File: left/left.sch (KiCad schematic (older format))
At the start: 41 parts, among them J1 Modulo-Jack, J2 Modulo-Jack, J3 Modulo-Jack, SW1 SW_Push, SW10 SW_Push, SW11 SW_Push, SW12 SW_Push, SW13 SW_Push, SW14 SW_Push, SW15 SW_Push, SW16 SW_Push, SW17 SW_Push, SW18 SW_Push, SW19 SW_Push, SW2 SW_Push, SW20 SW_Push, SW21 SW_Push, SW22 SW_Push, SW23 SW_Push, SW24 SW_Push, SW25 SW_Push, SW26 SW_Push, SW27 SW_Push, SW28 SW_Push, SW29 SW_Push, SW3 SW_Push, SW30 SW_Push, SW31 SW_Push, SW32 SW_SPDT, SW33 SW_SPDT, SW4 SW_Push, SW5 SW_Push, SW6 SW_Push, SW7 SW_Push, SW8 SW_Push, SW9 SW_Push, U1 MCP23017_SP, U2 MCP23017_SP

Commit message: left: change address switch to DPDT
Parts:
- removed SW32, SW33: SW_SPDT, lib:SlideSwitch_SS-12D00, symbol Switch:SW_SPDT
- added SW32, SW33: SW_DPDT_x2, lib:SlideSwitch_IS2235, symbol Switch:SW_DPDT_x2
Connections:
- net A1: now also SW32.2 (B)
- net A2: now also SW33.2 (B)
- net GND: now also SW32.3 (C), SW33.3 (C)
- net VCC: now also SW32.1 (A), SW33.1 (A)
- no-connect marks 6 -> 14
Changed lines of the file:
@@
 Wire Wire Line
 	2700 5600 3000 5600
-$Comp
-L Switch:SW_SPDT SW32
-U 1 1 5CF616F7
-P 1550 6800
-F 0 "SW32" H 1550 7085 50  0000 C CNN
-F 1 "SW_SPDT" H 1550 6994 50  0000 C CNN
-F 2 "lib:SlideSwitch_SS-12D00" H 1550 6800 50  0001 C CNN
-F 3 "~" H 1550 6800 50  0001 C CNN
-	1    1550 6800
-	1    0    0    -1
-$EndComp
 Text GLabel 1350 6800 0    50   Output ~ 0
 A1
@@
 F 3 "" H 1750 6900 50  0001 C CNN
 	1    1750 6900
-	1    0    0    -1
-$EndComp
-$Comp
-L Switch:SW_SPDT SW33
-U 1 1 5CF62A7C
-P 2300 6800
-F 0 "SW33" H 2300 7085 50  0000 C CNN
-F 1 "SW_SPDT" H 2300 6994 50  0000 C CNN
-F 2 "lib:SlideSwitch_SS-12D00" H 2300 6800 50  0001 C CNN
-F 3 "~" H 2300 6800 50  0001 C CNN
-	1    2300 6800
 	1    0    0    -1
 $EndComp
@@
 	1    0    0    -1
 $EndComp
+$Comp
+L Switch:SW_DPDT_x2 SW32
+U 1 1 5CF7FADE
+P 1550 6800
+F 0 "SW32" H 1550 7085 50  0000 C CNN
+F 1 "SW_DPDT_x2" H 1550 6994 50  0000 C CNN
+F 2 "lib:SlideSwitch_IS2235" H 1550 6800 50  0001 C CNN
+F 3 "~" H 1550 6800 50  0001 C CNN
+	1    1550 6800
+	1    0    0    -1
+$EndComp
+$Comp
+L Switch:SW_DPDT_x2 SW33
+U 1 1 5CF804A5
+P 2300 6800
+F 0 "SW33" H 2300 7085 50  0000 C CNN
+F 1 "SW_DPDT_x2" H 2300 6994 50  0000 C CNN
+F 2 "lib:SlideSwitch_IS2235" H 2300 6800 50  0001 C CNN
+F 3 "~" H 2300 6800 50  0001 C CNN
+	1    2300 6800
+	1    0    0    -1
+$EndComp
+$Comp
+L Switch:SW_DPDT_x2 SW32
+U 2 1 5CF84163
+P 1550 7400
+F 0 "SW32" H 1550 7685 50  0000 C CNN
+F 1 "SW_DPDT_x2" H 1550 7594 50  0000 C CNN
+F 2 "lib:SlideSwitch_IS2235" H 1550 7400 50  0001 C CNN
+F 3 "~" H 1550 7400 50  0001 C CNN
+	2    1550 7400
+	1    0    0    -1
+$EndComp
+$Comp
+L Switch:SW_DPDT_x2 SW33
+U 2 1 5CF853BA
+P 2300 7400
+F 0 "SW33" H 2300 7685 50  0000 C CNN
+F 1 "SW_DPDT_x2" H 2300 7594 50  0000 C CNN
+F 2 "lib:SlideSwitch_IS2235" H 2300 7400 50  0001 C CNN
+F 3 "~" H 2300 7400 50  0001 C CNN
+	2    2300 7400
+	1    0    0    -1
+$EndComp
+NoConn ~ 1350 7400
+NoConn ~ 1750 7500
+NoConn ~ 1750 7300
+NoConn ~ 2500 7300
+NoConn ~ 2500 7500
+NoConn ~ 2100 7400
+NoConn ~ 2700 4700
+NoConn ~ 1300 4700
 $EndSCHEMATC

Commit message: last commit
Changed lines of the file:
@@
 NoConn ~ 2700 4700
 NoConn ~ 1300 4700
+$Comp
+L power:VCC #PWR051
+U 1 1 5CF90F28
+P 3400 7250
+F 0 "#PWR051" H 3400 7100 50  0001 C CNN
+F 1 "VCC" H 3417 7423 50  0000 C CNN
+F 2 "" H 3400 7250 50  0001 C CNN
+F 3 "" H 3400 7250 50  0001 C CNN
+	1    3400 7250
+	1    0    0    -1
+$EndComp
+$Comp
+L power:GND #PWR052
+U 1 1 5CF9147D
+P 3750 7250
+F 0 "#PWR052" H 3750 7000 50  0001 C CNN
+F 1 "GND" H 3755 7077 50  0000 C CNN
+F 2 "" H 3750 7250 50  0001 C CNN
+F 3 "" H 3750 7250 50  0001 C CNN
+	1    3750 7250
+	1    0    0    -1
+$EndComp
+$Comp
+L power:PWR_FLAG #FLG02
+U 1 1 5CF91B6C
+P 3750 7250
+F 0 "#FLG02" H 3750 7325 50  0001 C CNN
+F 1 "PWR_FLAG" H 3750 7423 50  0000 C CNN
+F 2 "" H 3750 7250 50  0001 C CNN
+F 3 "~" H 3750 7250 50  0001 C CNN
+	1    3750 7250
+	1    0    0    -1
+$EndComp
+$Comp
+L power:PWR_FLAG #FLG01
+U 1 1 5CF921EF
+P 3400 7250
+F 0 "#FLG01" H 3400 7325 50  0001 C CNN
+F 1 "PWR_FLAG" H 3400 7423 50  0000 C CNN
+F 2 "" H 3400 7250 50  0001 C CNN
+F 3 "~" H 3400 7250 50  0001 C CNN
+	1    3400 7250
+	1    0    0    1
+$EndComp
+$Comp
+L power:PWR_FLAG #FLG0101
+U 1 1 5CF94E79
+P 4200 7250
+F 0 "#FLG0101" H 4200 7325 50  0001 C CNN
+F 1 "PWR_FLAG" H 4200 7423 50  0000 C CNN
+F 2 "" H 4200 7250 50  0001 C CNN
+F 3 "~" H 4200 7250 50  0001 C CNN
+	1    4200 7250
+	1    0    0    -1
+$EndComp
+Text GLabel 4200 7250 3    50   Input ~ 0
+SCL
 $EndSCHEMATC

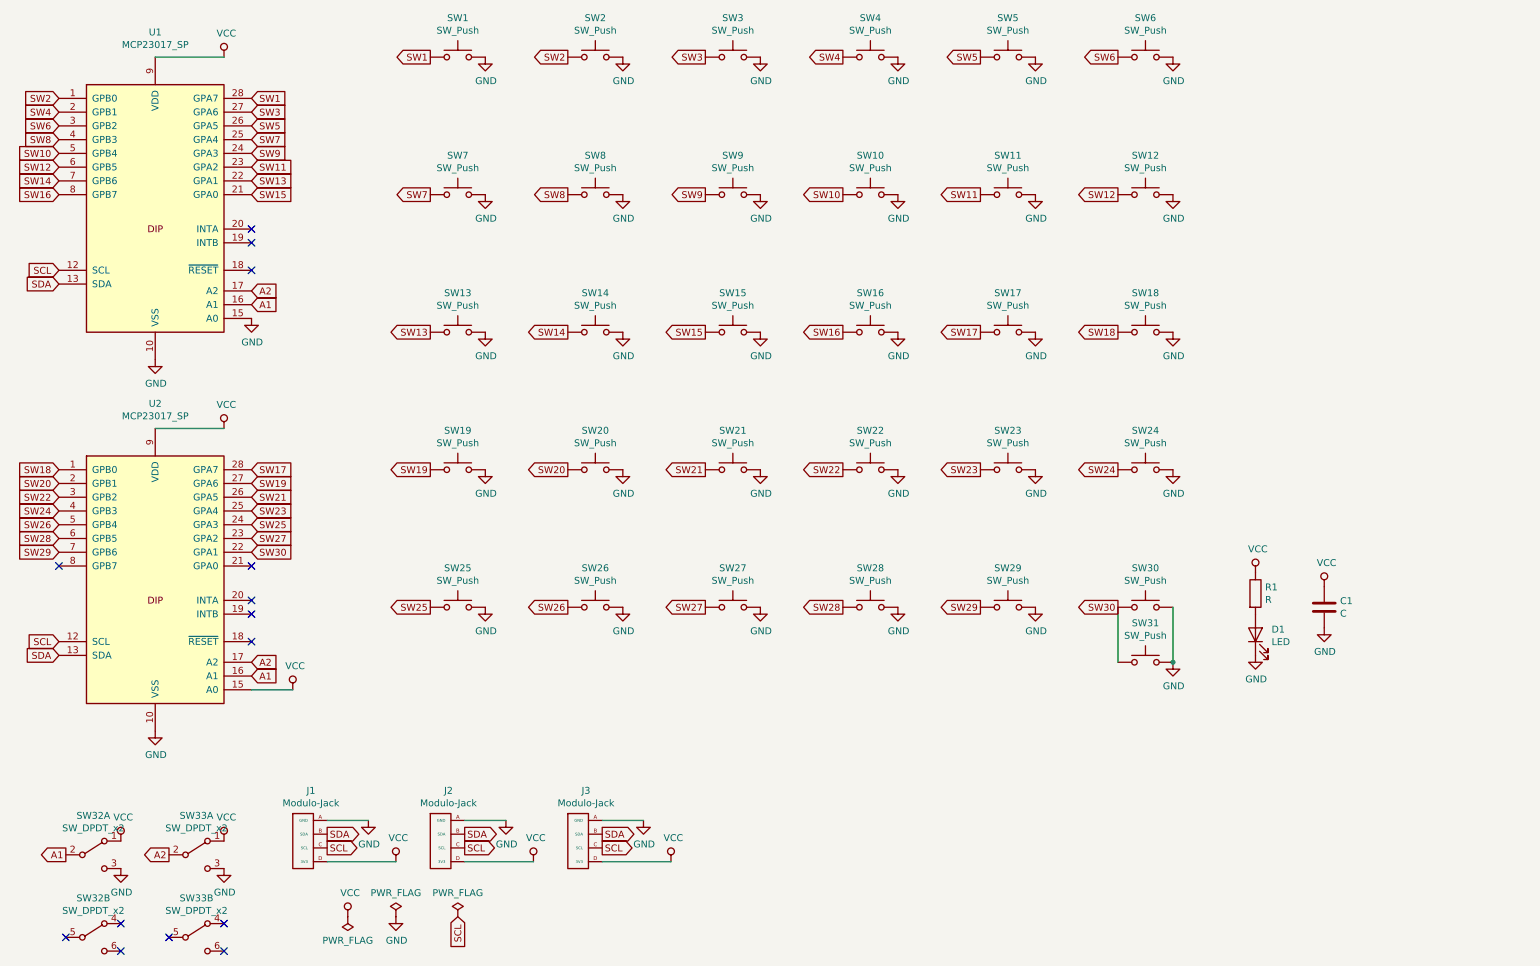
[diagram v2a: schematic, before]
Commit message: modify left to JIS layout
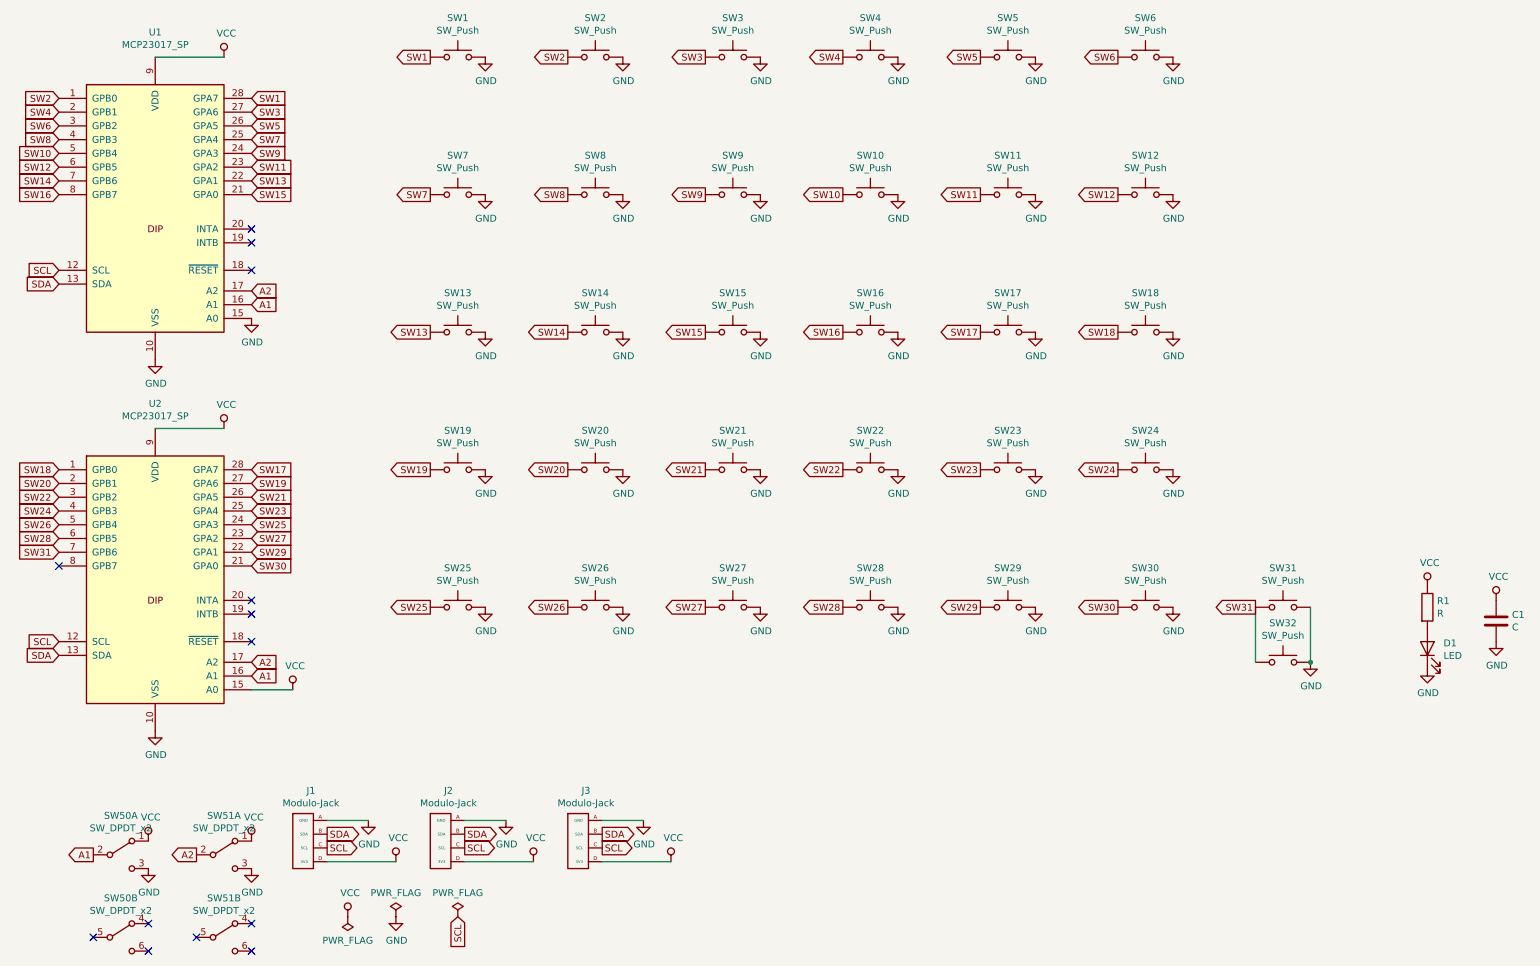
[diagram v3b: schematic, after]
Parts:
- added SW30: SW_Push, MX_Socket:MXOnly-1U-Hotswap, symbol Switch:SW_Push
- SW26: footprint MX_Socket:MXOnly-1.25U-Hotswap -> MX_Socket:MXOnly-1U-Hotswap
- renumbered SW30 to SW31, SW31 to SW32, SW32 to SW50, SW33 to SW51
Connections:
- net GND: now also SW31.1, SW32.1, SW30.1; no longer SW31.2, SW32.2
- net SW29: now also U2.22 (GPA1); no longer U2.7 (GPB6)
- net SW30: now also U2.21 (GPA0), SW30.2; no longer SW31.1, SW32.1, U2.22 (GPA1)
- new net SW31: SW31.2, SW32.2, U2.7 (GPB6)
- no-connect marks 14 -> 13
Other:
- moved on the sheet: C1, D1, R1, SW31, SW32, SW50A, SW50B, SW51A, SW51B
